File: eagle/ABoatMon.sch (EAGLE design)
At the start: 26 parts, among them J1 5V, J2 GND, J3 GND, J4 5V, X1 MKDSN1,5/3-5,08, X4 MKDSN1,5/2-5,08, X5 MKDSN1,5/3-5,08, X6 MKDSN1,5/3-5,08

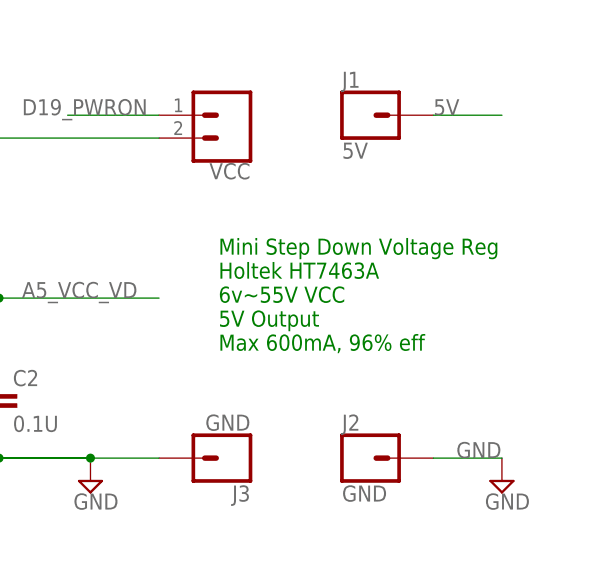
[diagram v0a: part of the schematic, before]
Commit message: Silkscreen improvements II
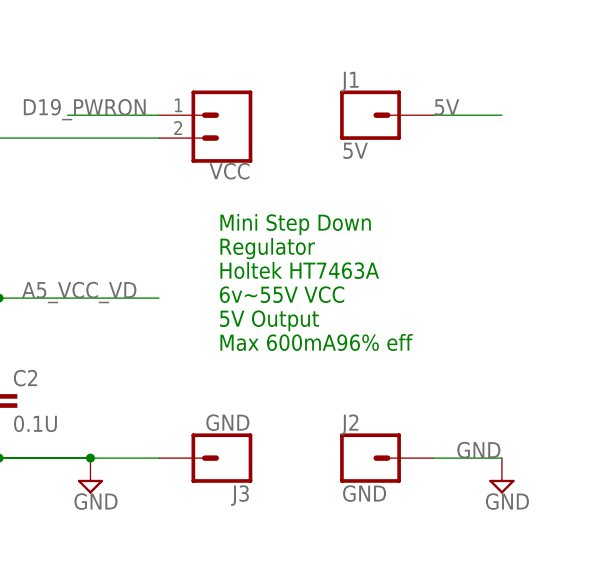
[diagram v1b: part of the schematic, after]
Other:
- note added: "Mini Step Down Regulator Holtek HT7463A 6v~55V VCC 5V Output Max 600mA96% eff"
- note removed: "Mini Step Down Voltage Reg Holtek HT7463A 6v~55V VCC 5V Output Max 600mA, 96% eff"
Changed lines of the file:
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@@
 <plain>
 <text x="11.684" y="146.558" size="1.778" layer="91">LIPO Voltage Divider/ADC</text>
-<text x="222.504" y="57.658" size="1.778" layer="91">Mini Step Down Voltage Reg
+<text x="222.504" y="57.658" size="1.778" layer="91">Mini Step Down
+Regulator
 Holtek HT7463A
 6v~55V VCC
 5V Output
-Max 600mA, 96% eff</text>
+Max 600mA96% eff</text>
 <text x="125.984" y="98.298" size="1.778" layer="91">Note: Need to remove the 10K pull resistor
  from the Enable pin to Volt Reg Enable

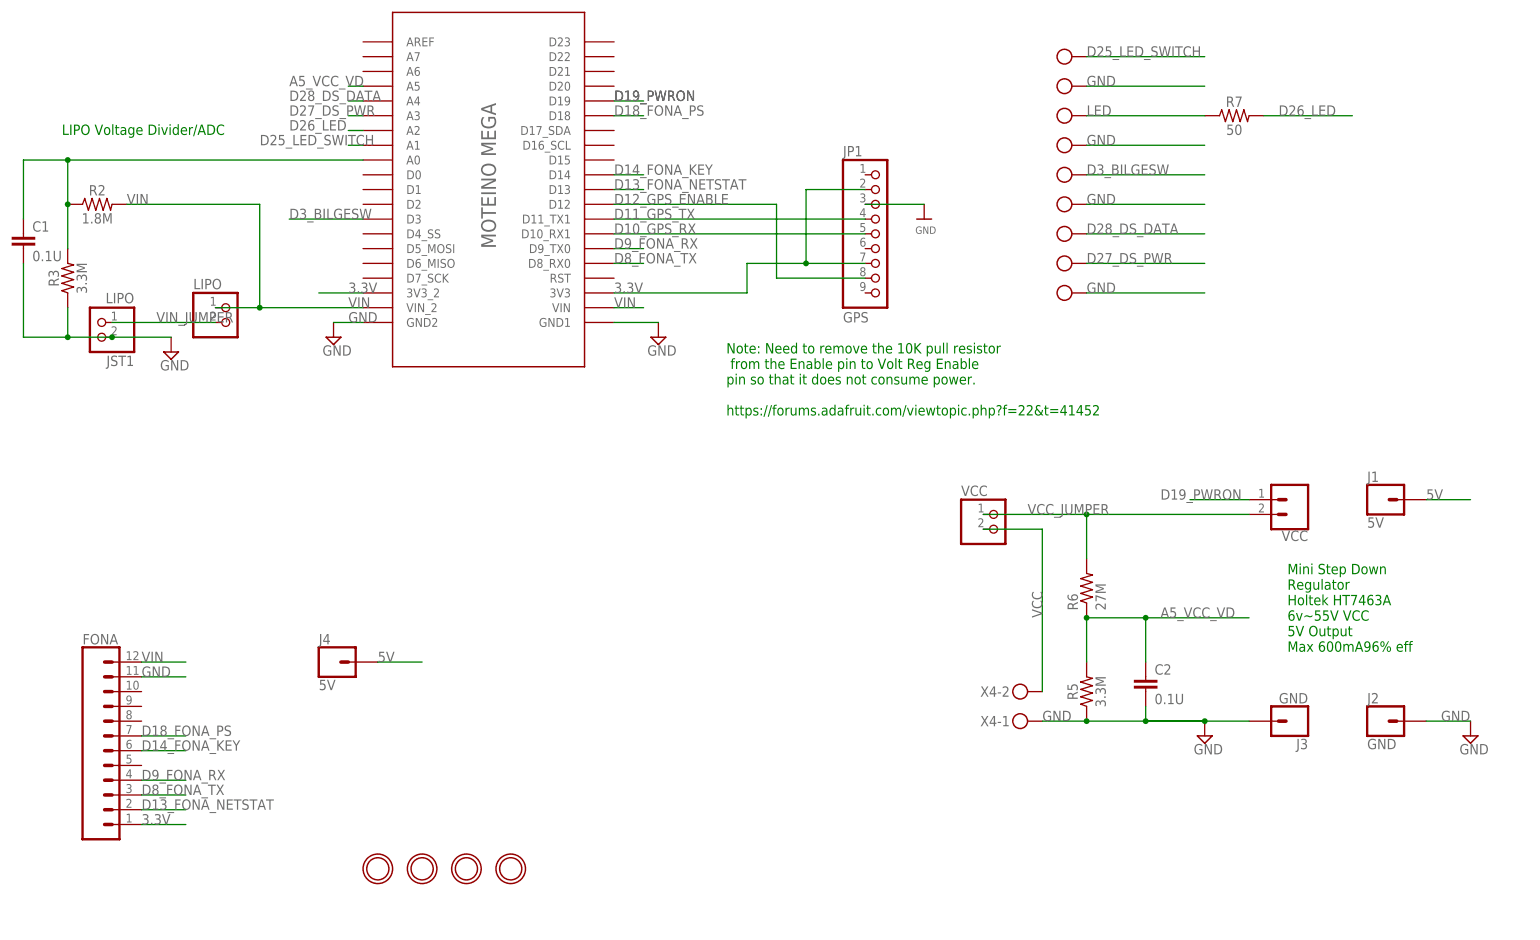
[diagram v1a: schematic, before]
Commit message: changed layout for sonoff box
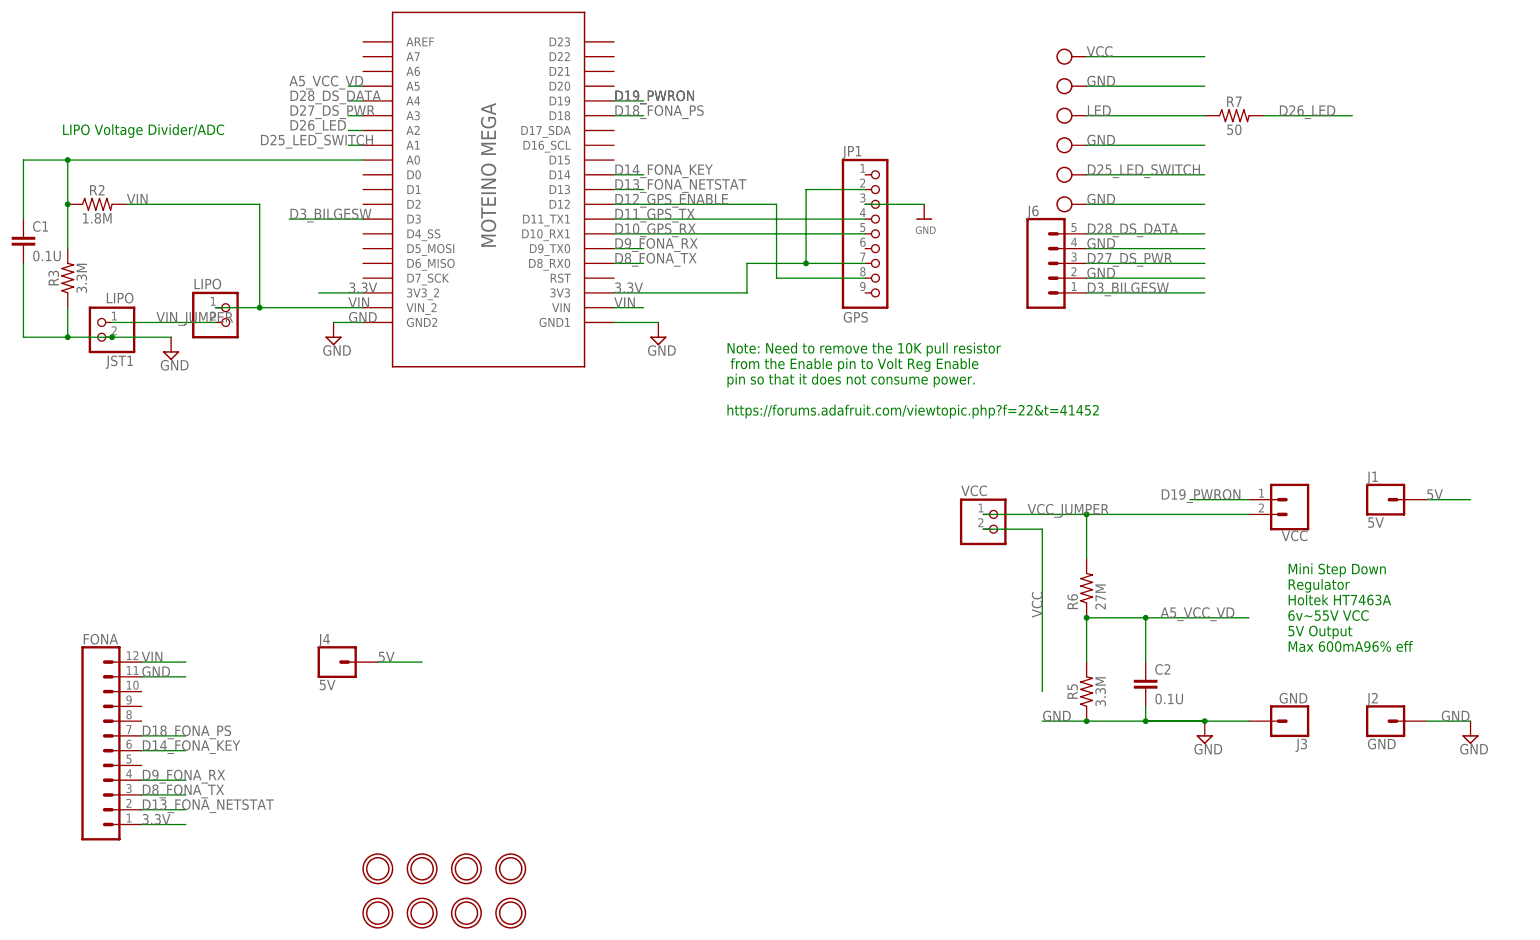
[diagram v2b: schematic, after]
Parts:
- removed X4: MKDSN1,5/2-5,08, con-phoenix-508:MKDSN1,5/2-5,08
- removed X5: MKDSN1,5/3-5,08, con-phoenix-508:MKDSN1,5/3-5,08
- added J6: (no value), SparkFun-Connectors:CONN_05JST
- added U$1, U$6, U$7, U$8: MOUNTINGHOLE2.5, microbuilder:MOUNTINGHOLE2.5
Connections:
- net D25_LED_SWITCH: now also X1-2.KL; no longer X6-1.KL
- net D27_DS_PWR: now also J6.3; no longer X5-2.KL
- net D28_DS_DATA: now also J6.5; no longer X5-3.KL
- net D3_BILGESW: now also J6.1; no longer X1-2.KL
- net GND: now also J6.2, J6.4; no longer X4-1.KL, X5-1.KL
- net VCC: now also X6-1.KL; no longer X4-2.KL
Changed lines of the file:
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@@
 <part name="LIPO" library="microbuilder" deviceset="HEADER-1X2" device="ROUND"/>
 <part name="J4" library="SparkFun-Connectors" deviceset="CONN_01" device="" value="5V"/>
-<part name="X4" library="con-phoenix-508" library_urn="urn:adsk.eagle:library:176" deviceset="MKDSN1,5/2-5,08" device="" package3d_urn="urn:adsk.eagle:package:9630/1"/>
 <part name="X6" library="con-phoenix-508" library_urn="urn:adsk.eagle:library:176" deviceset="MKDSN1,5/3-5,08" device="" package3d_urn="urn:adsk.eagle:package:9641/1"/>
 <part name="X1" library="con-phoenix-508" library_urn="urn:adsk.eagle:library:176" deviceset="MKDSN1,5/3-5,08" device="" package3d_urn="urn:adsk.eagle:package:9641/1"/>
-<part name="X5" library="con-phoenix-508" library_urn="urn:adsk.eagle:library:176" deviceset="MKDSN1,5/3-5,08" device="" package3d_urn="urn:adsk.eagle:package:9641/1">
-<attribute name="SPICEPREFIX" value="X"/>
-</part>
+<part name="J6" library="SparkFun-Connectors" library_urn="urn:adsk.eagle:library:513" deviceset="CONN_05" device="JST" package3d_urn="urn:adsk.eagle:package:38120/1"/>
+<part name="U$1" library="microbuilder" deviceset="MOUNTINGHOLE" device="2.5"/>
+<part name="U$6" library="microbuilder" deviceset="MOUNTINGHOLE" device="2.5"/>
+<part name="U$7" library="microbuilder" deviceset="MOUNTINGHOLE" device="2.5"/>
+<part name="U$8" library="microbuilder" deviceset="MOUNTINGHOLE" device="2.5"/>
 </parts>
 <sheets>
@@
 <attribute name="NAME" x="55.88" y="58.928" size="1.778" layer="95" font="vector"/>
 </instance>
-<instance part="X4" gate="-1" x="177.8" y="45.72" smashed="yes" rot="R180">
-<attribute name="NAME" x="174.752" y="46.609" size="1.778" layer="95" rot="R180"/>
-</instance>
-<instance part="X4" gate="-2" x="177.8" y="50.8" smashed="yes" rot="R180">
-<attribute name="NAME" x="174.752" y="51.689" size="1.778" layer="95" rot="R180"/>
-</instance>
 <instance part="X6" gate="-1" x="185.42" y="160.02" smashed="yes" rot="R180"/>
 <instance part="X6" gate="-2" x="185.42" y="154.94" smashed="yes" rot="R180"/>
@@
 <instance part="X1" gate="-2" x="185.42" y="139.7" smashed="yes" rot="R180"/>
 <instance part="X1" gate="-3" x="185.42" y="144.78" smashed="yes" rot="R180"/>
-<instance part="X5" gate="-1" x="185.42" y="119.38" smashed="yes" rot="R180"/>
-<instance part="X5" gate="-2" x="185.42" y="124.46" smashed="yes" rot="R180"/>
-<instance part="X5" gate="-3" x="185.42" y="129.54" smashed="yes" rot="R180"/>
+<instance part="J6" gate="G$1" x="180.34" y="124.46" smashed="yes">
+<attribute name="VALUE" x="177.8" y="114.554" size="1.778" layer="96" font="vector"/>
+<attribute name="NAME" x="177.8" y="132.588" size="1.778" layer="95" font="vector"/>
+</instance>
+<instance part="U$1" gate="G$1" x="66.04" y="12.7" smashed="yes"/>
+<instance part="U$6" gate="G$1" x="73.66" y="12.7" smashed="yes"/>
+<instance part="U$7" gate="G$1" x="81.28" y="12.7" smashed="yes"/>
+<instance part="U$8" gate="G$1" x="88.9" y="12.7" smashed="yes"/>
 </instances>
 <busses>
@@
 <junction x="198.12" y="45.72"/>
 <pinref part="J3" gate="G$1" pin="1"/>
-<pinref part="X4" gate="-1" pin="KL"/>
 </segment>
 <segment>
@@
 </segment>
 <segment>
-<wire x1="187.96" y1="154.94" x2="208.28" y2="154.94" width="0.1524" layer="91"/>
-<label x="187.96" y="154.94" size="1.778" layer="95"/>
-<pinref part="X6" gate="-2" pin="KL"/>
-</segment>
-<segment>
-<wire x1="187.96" y1="144.78" x2="208.28" y2="144.78" width="0.1524" layer="91"/>
-<label x="187.96" y="144.78" size="1.778" layer="95"/>
-<pinref part="X1" gate="-3" pin="KL"/>
-</segment>
-<segment>
-<wire x1="187.96" y1="134.62" x2="208.28" y2="134.62" width="0.1524" layer="91"/>
-<label x="187.96" y="134.62" size="1.778" layer="95"/>
-<pinref part="X1" gate="-1" pin="KL"/>
-</segment>
-<segment>
-<wire x1="187.96" y1="119.38" x2="208.28" y2="119.38" width="0.1524" layer="91"/>
-<label x="187.96" y="119.38" size="1.778" layer="95"/>
-<pinref part="X5" gate="-1" pin="KL"/>
-</segment>
-<segment>
 <pinref part="FONA" gate="G$1" pin="11"/>
 <wire x1="25.4" y1="53.34" x2="33.02" y2="53.34" width="0.1524" layer="91"/>
@@
 <label x="60.96" y="114.3" size="1.778" layer="95"/>
 <pinref part="SUPPLY3" gate="GND" pin="GND"/>
+</segment>
+<segment>
+<pinref part="X6" gate="-2" pin="KL"/>
+<wire x1="187.96" y1="154.94" x2="208.28" y2="154.94" width="0.1524" layer="91"/>
+<label x="187.96" y="154.94" size="1.778" layer="95"/>
+</segment>
+<segment>
+<pinref part="X1" gate="-1" pin="KL"/>
+<wire x1="187.96" y1="134.62" x2="208.28" y2="134.62" width="0.1524" layer="91"/>
+<label x="187.96" y="134.62" size="1.778" layer="95"/>
+</segment>
+<segment>
+<wire x1="187.96" y1="121.92" x2="208.28" y2="121.92" width="0.1524" layer="91"/>
+<label x="187.96" y="121.92" size="1.778" layer="95"/>
+<pinref part="J6" gate="G$1" pin="2"/>
+</segment>
+<segment>
+<pinref part="X1" gate="-3" pin="KL"/>
+<wire x1="187.96" y1="144.78" x2="208.28" y2="144.78" width="0.1524" layer="91"/>
+<label x="187.96" y="144.78" size="1.778" layer="95"/>
+</segment>
+<segment>
+<wire x1="187.96" y1="127" x2="208.28" y2="127" width="0.1524" layer="91"/>
+<label x="187.96" y="127" size="1.778" layer="95"/>
+<pinref part="J6" gate="G$1" pin="4"/>
 </segment>
 </net>
@@
 <pinref part="VCC" gate="G$1" pin="2"/>
 <wire x1="170.18" y1="78.74" x2="180.34" y2="78.74" width="0.1524" layer="91"/>
-<pinref part="X4" gate="-2" pin="KL"/>
+</segment>
+<segment>
+<pinref part="X6" gate="-1" pin="KL"/>
+<wire x1="187.96" y1="160.02" x2="208.28" y2="160.02" width="0.1524" layer="91"/>
+<label x="187.96" y="160.02" size="1.778" layer="95"/>
 </segment>
 </net>
@@
 <net name="D25_LED_SWITCH" class="0">
 <segment>
-<wire x1="187.96" y1="160.02" x2="208.28" y2="160.02" width="0.1524" layer="91"/>
-<label x="187.96" y="160.02" size="1.778" layer="95"/>
-<pinref part="X6" gate="-1" pin="KL"/>
-</segment>
-<segment>
 <pinref part="MOTEINO_MEGA" gate="G$1" pin="A1"/>
 <wire x1="60.96" y1="144.78" x2="63.5" y2="144.78" width="0.1524" layer="91"/>
 <label x="45.72" y="144.78" size="1.778" layer="95"/>
 </segment>
-</net>
-<net name="D3_BILGESW" class="0">
-<segment>
+<segment>
+<pinref part="X1" gate="-2" pin="KL"/>
 <wire x1="187.96" y1="139.7" x2="208.28" y2="139.7" width="0.1524" layer="91"/>
 <label x="187.96" y="139.7" size="1.778" layer="95"/>
-<pinref part="X1" gate="-2" pin="KL"/>
-</segment>
+</segment>
+</net>
+<net name="D3_BILGESW" class="0">
 <segment>
 <pinref part="MOTEINO_MEGA" gate="G$1" pin="D3"/>
@@
 <label x="50.8" y="132.08" size="1.778" layer="95"/>
 </segment>
+<segment>
+<wire x1="187.96" y1="119.38" x2="208.28" y2="119.38" width="0.1524" layer="91"/>
+<label x="187.96" y="119.38" size="1.778" layer="95"/>
+<pinref part="J6" gate="G$1" pin="1"/>
+</segment>
 </net>
 <net name="D28_DS_DATA" class="0">
@@
 <wire x1="187.96" y1="129.54" x2="208.28" y2="129.54" width="0.1524" layer="91"/>
 <label x="187.96" y="129.54" size="1.778" layer="95"/>
-<pinref part="X5" gate="-3" pin="KL"/>
+<pinref part="J6" gate="G$1" pin="5"/>
 </segment>
 <segment>
@@
 <wire x1="187.96" y1="124.46" x2="208.28" y2="124.46" width="0.1524" layer="91"/>
 <label x="187.96" y="124.46" size="1.778" layer="95"/>
-<pinref part="X5" gate="-2" pin="KL"/>
-</segment>
-</net>
+<pinref part="J6" gate="G$1" pin="3"/>
+</segment>
+</net>

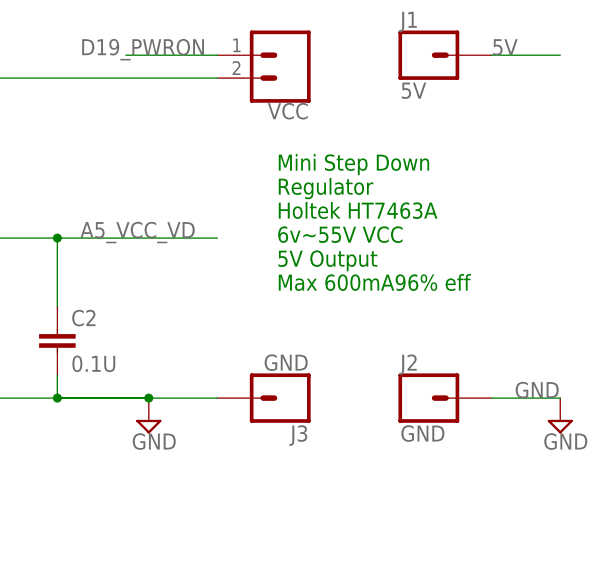
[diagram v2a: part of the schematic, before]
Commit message: Moved boxmounting holes 3mm
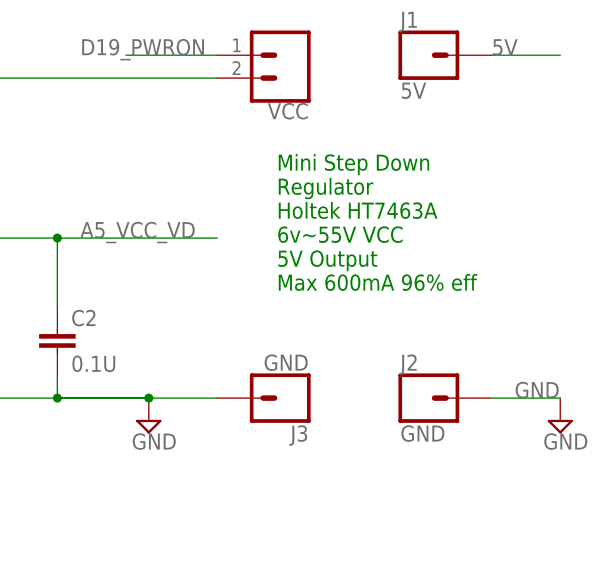
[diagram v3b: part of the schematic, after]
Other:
- note added: "Mini Step Down Regulator Holtek HT7463A 6v~55V VCC 5V Output Max 600mA 96% eff"
- note removed: "Mini Step Down Regulator Holtek HT7463A 6v~55V VCC 5V Output Max 600mA96% eff"
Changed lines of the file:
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@@
 <attributes>
 <attribute name="CNAME" value="MoteinoMega ABoatMon Shield"/>
-<attribute name="CREVISION" value="0.699"/>
+<attribute name="CREVISION" value="0.799"/>
 <attribute name="DESIGNER" value="gregcope@gmail.com"/>
 </attributes>
@@
 6v~55V VCC
 5V Output
-Max 600mA96% eff</text>
+Max 600mA 96% eff</text>
 <text x="125.984" y="98.298" size="1.778" layer="91">Note: Need to remove the 10K pull resistor
  from the Enable pin to Volt Reg Enable

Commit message: starting again
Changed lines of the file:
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@@
 <junction x="12.7" y="134.62"/>
 <pinref part="R3" gate="G$1" pin="2"/>
+<label x="45.72" y="142.24" size="1.778" layer="95"/>
 </segment>
 </net>
